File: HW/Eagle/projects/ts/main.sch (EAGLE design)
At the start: 0 parts

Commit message: Designed power supply
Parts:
- added C1, C2, C3: 100nF, rcl:C-EUC0805
- added C4, C5: 15pF, rcl:C-EUC0805
- added C6: 100uF, rcl:CPOL-EUTAP5-80
- added C7: 1000uF, rcl:CPOL-EUTT5D10
- added D1: 1N582X, misc:1N582X
- added ICSP: (no value), con-lstb:MA03-2
- added L1: 100uH, rcl:L-USTJ3-U1
- added Q1: (no value), crystal:CRYSTALHC49S
- added R1: 10k, rcl:R-EU_R0805
- added R2: 1M, rcl:R-EU_R0805
- added R3: 0, rcl:R-EU_R0805
- added U1: ATMEGA328P-PU, ATMEGA328P-PU:ATMEGA328P-PU
- added U2: LM2576T, misc:LM2576T
- added X1, X2: (no value), con-wago-500:W237-102
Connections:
- new net +12V: C6.+, U2.IN, X1-1.KL
- new net GND: C1.2, C2.1, C3.1, C4.1, C5.1, C6.-, C7.-, D1.A, ICSP.6, U1.GND, U1.GND_2, U2.!ON, U2.GND, X1-2.KL
- new net N$1: C1.1, U1.AREF
- new net N$2: ICSP.1, U1.PB4
- new net N$3: C5.2, Q1.1, R2.1, U1.PB7
- new net N$4: C4.2, Q1.2, R2.2, U1.PB6
- new net N$5: ICSP.3, U1.PB5
- new net N$6: ICSP.4, U1.PB3
- new net N$7: D1.C, L1.2, U2.OUT
- new net N$8: C7.+, L1.1, R3.1, U2.FEEDBACK
- new net NRST: ICSP.5, R1.1, U1.PC6
- new net VCC: C2.2, C3.2, ICSP.2, R3.2, U1.AVCC, U1.VCC

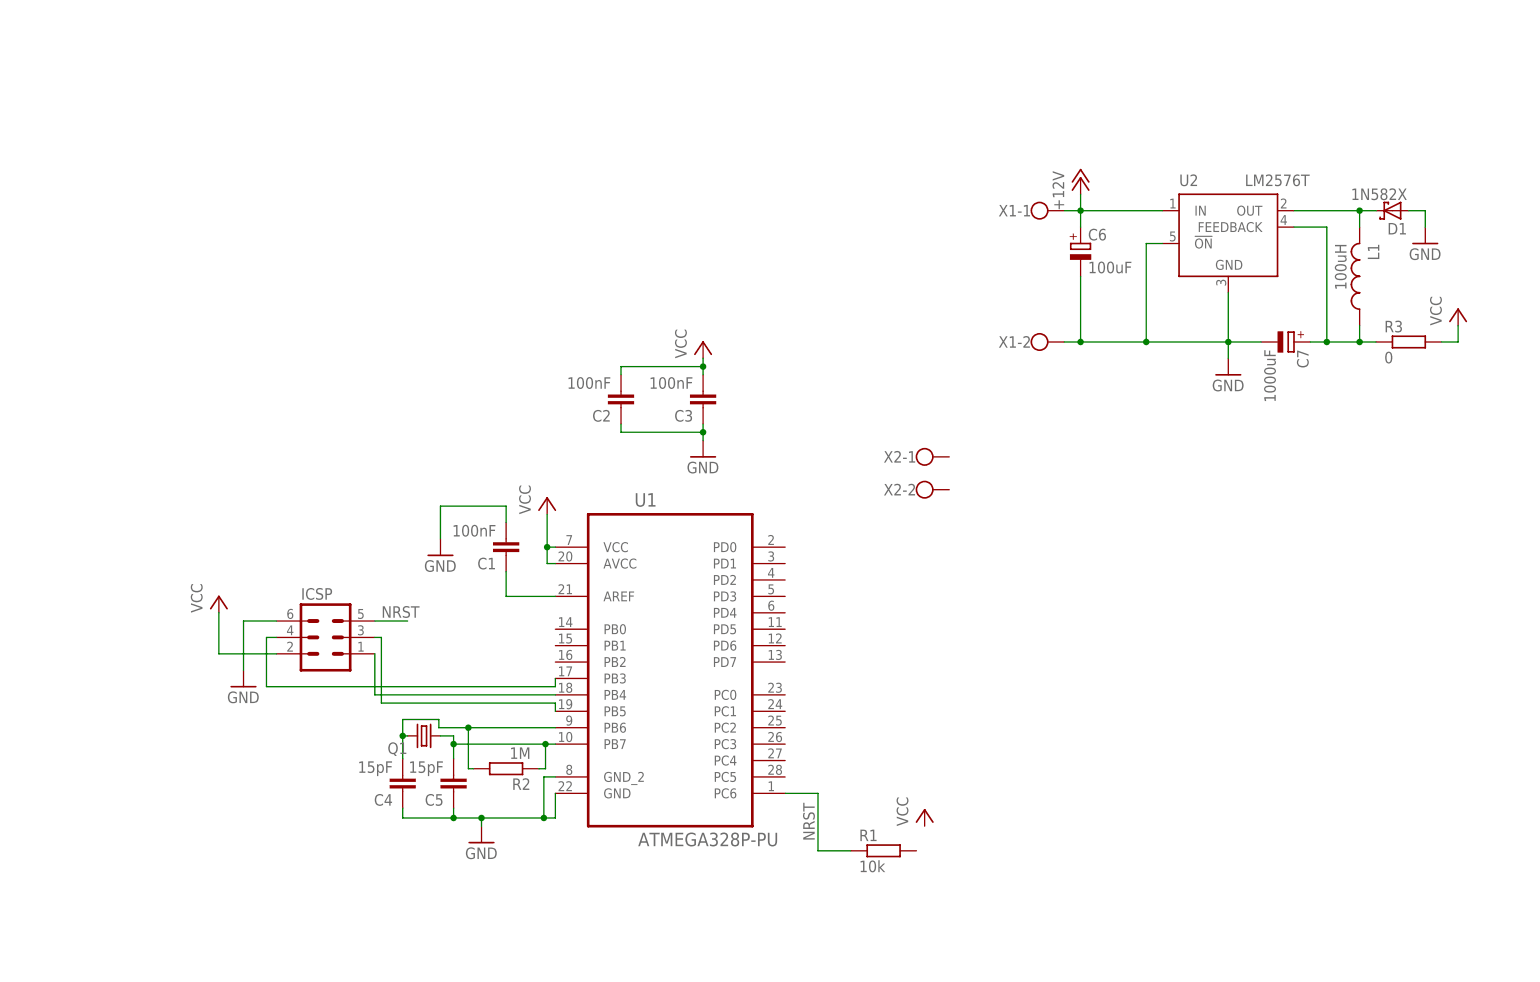
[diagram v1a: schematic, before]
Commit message: 3.3v supply
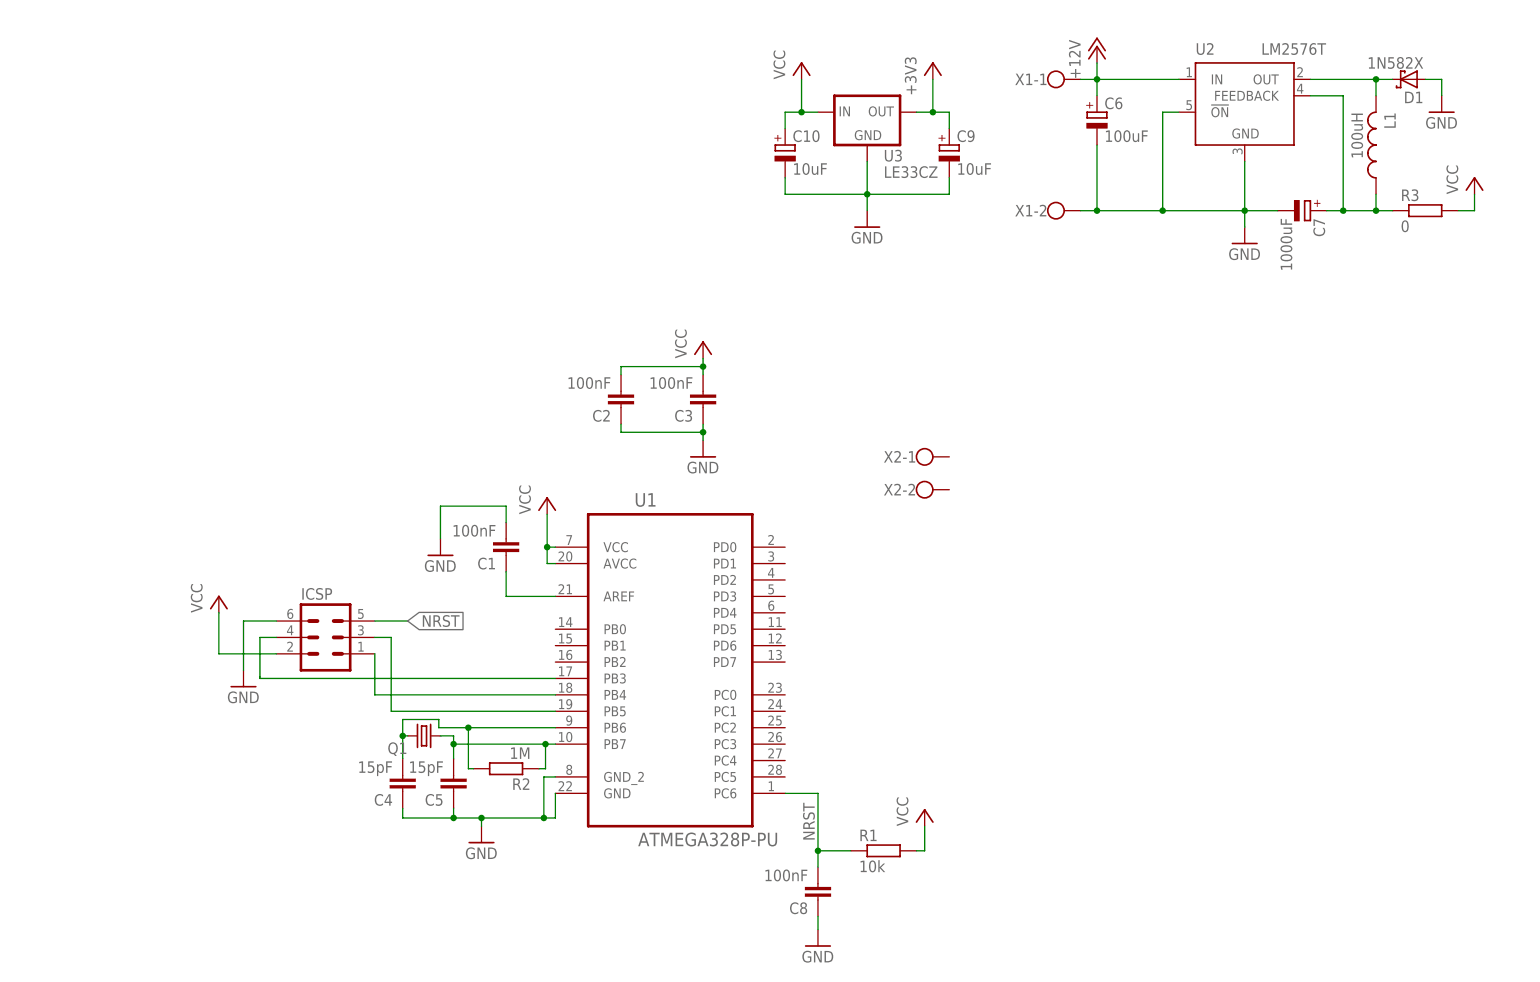
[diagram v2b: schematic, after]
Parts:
- added C10, C9: 10uF, rcl:CPOL-EUC
- added C8: 100nF, rcl:C-EUC0805
- added U3: LE33CZ, v-reg:LE33CZ
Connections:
- new net +3V3: C9.+, U3.OUT
- net GND: now also C10.-, C8.1, C9.-, U3.GND
- net NRST: now also C8.2
- net VCC: now also C10.+, R1.2, U3.IN
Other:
- moved on the sheet: C6, C7, D1, L1, R3, U2, X1-1, X1-2

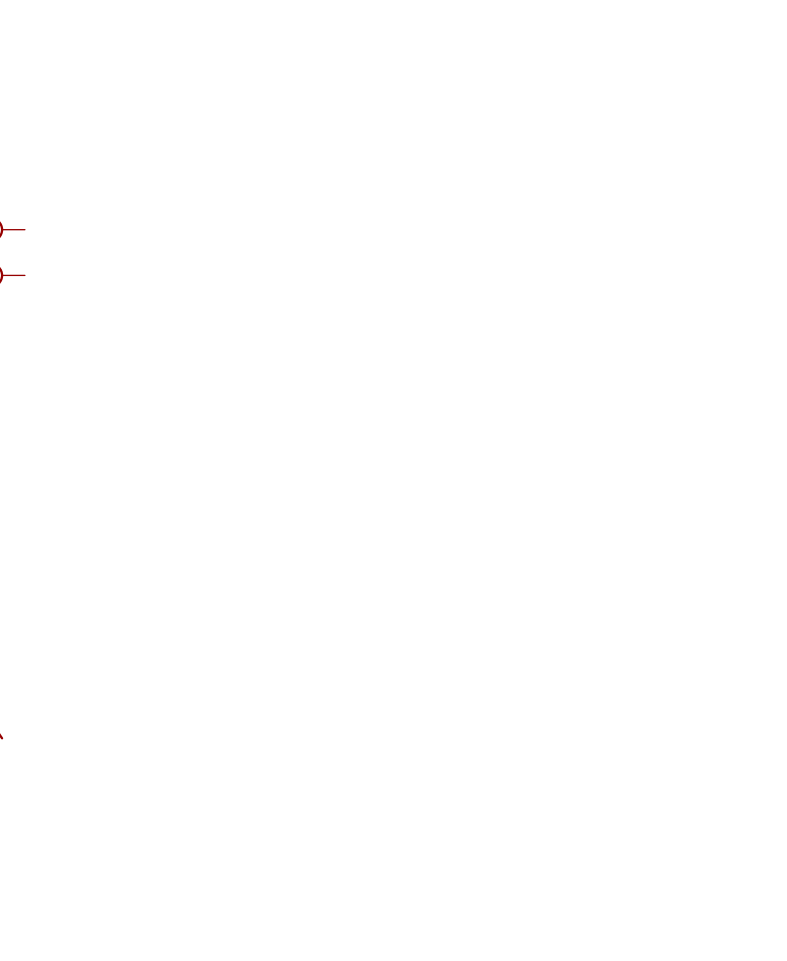
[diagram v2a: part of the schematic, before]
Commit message: Added level shifter CMOS 4050
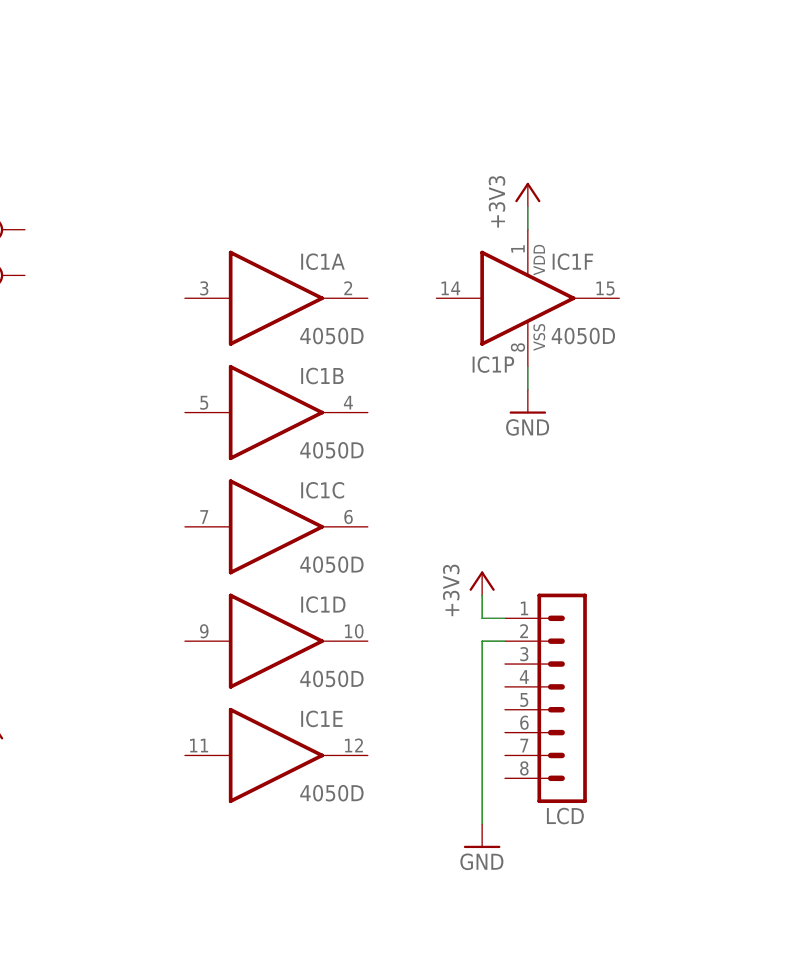
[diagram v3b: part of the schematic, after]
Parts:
- added IC1: 4050D, 40xx:4050D
- added LCD: (no value), con-lstb:MA08-1
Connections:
- net +3V3: now also IC1P.VDD, LCD.1
- net GND: now also IC1P.VSS, LCD.2
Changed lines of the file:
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@@
 <part name="C9" library="rcl" deviceset="CPOL-EU" device="C" value="10uF"/>
 <part name="C10" library="rcl" deviceset="CPOL-EU" device="C" value="10uF"/>
+<part name="IC1" library="40xx" deviceset="4050" device="D"/>
+<part name="GND9" library="supply1" deviceset="GND" device=""/>
+<part name="+3V2" library="supply1" deviceset="+3V3" device=""/>
+<part name="LCD" library="con-lstb" deviceset="MA08-1" device=""/>
+<part name="+3V3" library="supply1" deviceset="+3V3" device=""/>
+<part name="GND10" library="supply1" deviceset="GND" device=""/>
 </parts>
 <sheets>
@@
 <instance part="C9" gate="G$1" x="165.1" y="149.86"/>
 <instance part="C10" gate="G$1" x="139.7" y="149.86"/>
+<instance part="IC1" gate="A" x="193.04" y="93.98"/>
+<instance part="IC1" gate="B" x="193.04" y="81.28"/>
+<instance part="IC1" gate="C" x="193.04" y="68.58"/>
+<instance part="IC1" gate="D" x="193.04" y="55.88"/>
+<instance part="IC1" gate="E" x="193.04" y="43.18"/>
+<instance part="IC1" gate="F" x="220.98" y="93.98"/>
+<instance part="IC1" gate="P" x="220.98" y="93.98" smashed="yes">
+<attribute name="NAME" x="214.63" y="85.725" size="1.778" layer="95"/>
+</instance>
+<instance part="GND9" gate="1" x="220.98" y="81.28"/>
+<instance part="+3V2" gate="G$1" x="220.98" y="106.68"/>
+<instance part="LCD" gate="1" x="226.06" y="50.8" rot="R180"/>
+<instance part="+3V3" gate="G$1" x="215.9" y="63.5"/>
+<instance part="GND10" gate="1" x="215.9" y="33.02"/>
 </instances>
 <busses>
@@
 <junction x="152.4" y="142.24"/>
 </segment>
+<segment>
+<pinref part="IC1" gate="P" pin="VSS"/>
+<pinref part="GND9" gate="1" pin="GND"/>
+<wire x1="220.98" y1="86.36" x2="220.98" y2="83.82" width="0.1524" layer="91"/>
+</segment>
+<segment>
+<pinref part="LCD" gate="1" pin="2"/>
+<pinref part="GND10" gate="1" pin="GND"/>
+<wire x1="218.44" y1="55.88" x2="215.9" y2="55.88" width="0.1524" layer="91"/>
+<wire x1="215.9" y1="55.88" x2="215.9" y2="35.56" width="0.1524" layer="91"/>
+</segment>
 </net>
 <net name="VCC" class="0">
@@
 <junction x="162.56" y="154.94"/>
 </segment>
-</net>
+<segment>
+<pinref part="IC1" gate="P" pin="VDD"/>
+<pinref part="+3V2" gate="G$1" pin="+3V3"/>
+<wire x1="220.98" y1="101.6" x2="220.98" y2="104.14" width="0.1524" layer="91"/>
+</segment>
+<segment>
+<pinref part="LCD" gate="1" pin="1"/>
+<pinref part="+3V3" gate="G$1" pin="+3V3"/>
+<wire x1="218.44" y1="58.42" x2="215.9" y2="58.42" width="0.1524" layer="91"/>
+<wire x1="215.9" y1="58.42" x2="215.9" y2="60.96" width="0.1524" layer="91"/>
+</segment>
+</net>

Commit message: Many changes
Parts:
- added C11: 100nF, rcl:C-EUC0805
- added L2: 10uH, misc:FERRCORE
- added R4: 330R, rcl:R-EU_R0805
- added R5: 0R, rcl:R-EU_R0805
- added RESET: (no value), switch-omron:10-XX
- R3: value 0 -> 0R
- U3: value LE33CZ -> HT7533
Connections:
- net N$1 renamed AREF
- net N$2 renamed MISO
- removed net N$5: ICSP.3, U1.PB5
- removed net N$6: ICSP.4, U1.PB3
- new net AVCC: C2.2, L2.1, U1.AVCC
- new net LCD_DC: IC1F.O, LCD.5
- new net LCD_LED: LCD.8, R4.2
- new net LCD_MOSI: IC1E.O, LCD.6
- new net LCD_RST: IC1B.O, LCD.4
- new net LCD_SCE: IC1A.O, LCD.3
- new net LCD_SCK: IC1D.O, LCD.7
- new net MOSI: IC1E.I, ICSP.4, U1.PB3
- new net N$1: C9.+, R5.2, U3.OUT
- new net N$2: R4.1
- new net RXD: U1.PD0
- new net SCK: IC1D.I, ICSP.3, U1.PB5
- new net TXD: U1.PD1
- net +3V3: now also C11.2, R5.1; no longer C9.+, U3.OUT
- net GND: now also C11.1, IC1C.I, RESET.P
- net NRST: now also RESET.S
- net VCC: now also L2.2; no longer C2.2, U1.AVCC
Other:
- moved on the sheet: C2, IC1A, IC1B, IC1C, IC1D, IC1E, IC1F, IC1P, LCD, X2-1, X2-2
